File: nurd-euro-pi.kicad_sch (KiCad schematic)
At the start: 45 parts, among them J1 RPi_GPIO, J2 AudioJack2, J3 AudioJack2, J4 AudioJack2, J5 AudioJack2, J6 AudioJack2, J7 AudioJack2, Q1 2N3904, Q2 2N3904, U1 tl072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

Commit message: descriptions
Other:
- note added: "+/-5 => 0...3.3V"
- note added: "0...3 => +/- 5V"
- note added: "0/5V => 0/3.3V (don't break on -5V)"
- note added: "generate -5V"
- title: (none) -> Eurocrack Hat
- moved on the sheet: U6C
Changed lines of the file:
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@@
 (kicad_sch (version 20211123) (generator eeschema)
   (paper "A4")
+  (title_block
+    (title "Eurocrack Hat")
+  )
   (junction (at 78.74 33.02) (diameter 0) (color 0 0 0 0)
   )
@@
   (wire (pts (xy 74.93 87.63) (xy 80.01 87.63))
     (stroke (width 0) (type default) (color 0 0 0 0))
+  )
+  (text "generate -5V" (at 58.42 73.66 0)
+    (effects (font (size 1.27 1.27)) (justify left bottom))
+  )
+  (text "0...3 => +/- 5V" (at 55.88 146.05 0)
+    (effects (font (size 1.27 1.27)) (justify left bottom))
+  )
+  (text "0/5V => 0/3.3V (don't break on -5V)" (at 134.62 157.48 0)
+    (effects (font (size 1.27 1.27)) (justify left bottom))
+  )
+  (text "+/-5 => 0...3.3V" (at 60.96 16.51 0)
+    (effects (font (size 1.27 1.27)) (justify left bottom))
   )
   (symbol (lib_id "power:GND") (at 242.57 95.25 90) (unit 1)
@@
     (pin "2")
   )
-  (symbol (lib_id "Amplifier_Operational:MCP6002-xP") (at 193.04 27.94 0) (unit 3)
-    (in_bom yes) (on_board yes) (fields_autoplaced)
-    (property "Reference" "U6" (id 0) (at 191.77 26.6699 0)
-      (effects (font (size 1.27 1.27)) (justify left))
-    )
-    (property "Value" "tl072" (id 1) (at 191.77 29.2099 0)
-      (effects (font (size 1.27 1.27)) (justify left))
-    )
-    (property "Footprint" "Package_DIP:DIP-8_W7.62mm_Socket_LongPads" (id 2) (at 193.04 27.94 0)
-      (effects (font (size 1.27 1.27)) hide)
-    )
-    (property "Datasheet" "http://ww1.microchip.com/downloads/en/DeviceDoc/21733j.pdf" (id 3) (at 193.04 27.94 0)
+  (symbol (lib_id "Amplifier_Operational:MCP6002-xP") (at 92.71 24.13 90) (unit 3)
+    (in_bom yes) (on_board yes) (fields_autoplaced)
+    (property "Reference" "U6" (id 0) (at 91.4399 25.4 0)
+      (effects (font (size 1.27 1.27)) (justify left))
+    )
+    (property "Value" "tl072" (id 1) (at 93.9799 25.4 0)
+      (effects (font (size 1.27 1.27)) (justify left))
+    )
+    (property "Footprint" "Package_DIP:DIP-8_W7.62mm_Socket_LongPads" (id 2) (at 92.71 24.13 0)
+      (effects (font (size 1.27 1.27)) hide)
+    )
+    (property "Datasheet" "http://ww1.microchip.com/downloads/en/DeviceDoc/21733j.pdf" (id 3) (at 92.71 24.13 0)
       (effects (font (size 1.27 1.27)) hide)
     )
@@
     (pin "1")
   )
-  (symbol (lib_id "power:GND") (at 190.5 35.56 0) (unit 1)
-    (in_bom yes) (on_board yes) (fields_autoplaced)
-    (property "Reference" "#PWR0145" (id 0) (at 190.5 41.91 0)
-      (effects (font (size 1.27 1.27)) hide)
-    )
-    (property "Value" "GND" (id 1) (at 193.04 36.8299 0)
-      (effects (font (size 1.27 1.27)) (justify left))
-    )
-    (property "Footprint" "" (id 2) (at 190.5 35.56 0)
-      (effects (font (size 1.27 1.27)) hide)
-    )
-    (property "Datasheet" "" (id 3) (at 190.5 35.56 0)
+  (symbol (lib_id "power:GND") (at 100.33 26.67 90) (unit 1)
+    (in_bom yes) (on_board yes) (fields_autoplaced)
+    (property "Reference" "#PWR0145" (id 0) (at 106.68 26.67 0)
+      (effects (font (size 1.27 1.27)) hide)
+    )
+    (property "Value" "GND" (id 1) (at 101.5999 24.13 0)
+      (effects (font (size 1.27 1.27)) (justify left))
+    )
+    (property "Footprint" "" (id 2) (at 100.33 26.67 0)
+      (effects (font (size 1.27 1.27)) hide)
+    )
+    (property "Datasheet" "" (id 3) (at 100.33 26.67 0)
       (effects (font (size 1.27 1.27)) hide)
     )
@@
     (pin "8")
   )
-  (symbol (lib_id "power:+3.3V") (at 190.5 20.32 0) (unit 1)
-    (in_bom yes) (on_board yes) (fields_autoplaced)
-    (property "Reference" "#PWR0144" (id 0) (at 190.5 24.13 0)
-      (effects (font (size 1.27 1.27)) hide)
-    )
-    (property "Value" "+3.3V" (id 1) (at 193.04 19.0499 0)
-      (effects (font (size 1.27 1.27)) (justify left))
-    )
-    (property "Footprint" "" (id 2) (at 190.5 20.32 0)
-      (effects (font (size 1.27 1.27)) hide)
-    )
-    (property "Datasheet" "" (id 3) (at 190.5 20.32 0)
-      (effects (font (size 1.27 1.27)) hide)
-    )
+  (symbol (lib_id "power:+3.3V") (at 85.09 26.67 90) (unit 1)
+    (in_bom yes) (on_board yes) (fields_autoplaced)
+    (property "Reference" "#PWR0144" (id 0) (at 88.9 26.67 0)
+      (effects (font (size 1.27 1.27)) hide)
+    )
+    (property "Value" "+3.3V" (id 1) (at 83.8199 24.13 0)
+      (effects (font (size 1.27 1.27)) (justify left))
+    )
+    (property "Footprint" "" (id 2) (at 85.09 26.67 0)
+      (effects (font (size 1.27 1.27)) hide)
+    )
+    (property "Datasheet" "" (id 3) (at 85.09 26.67 0)
+      (effects (font (size 1.27 1.27)) hide)
+    )

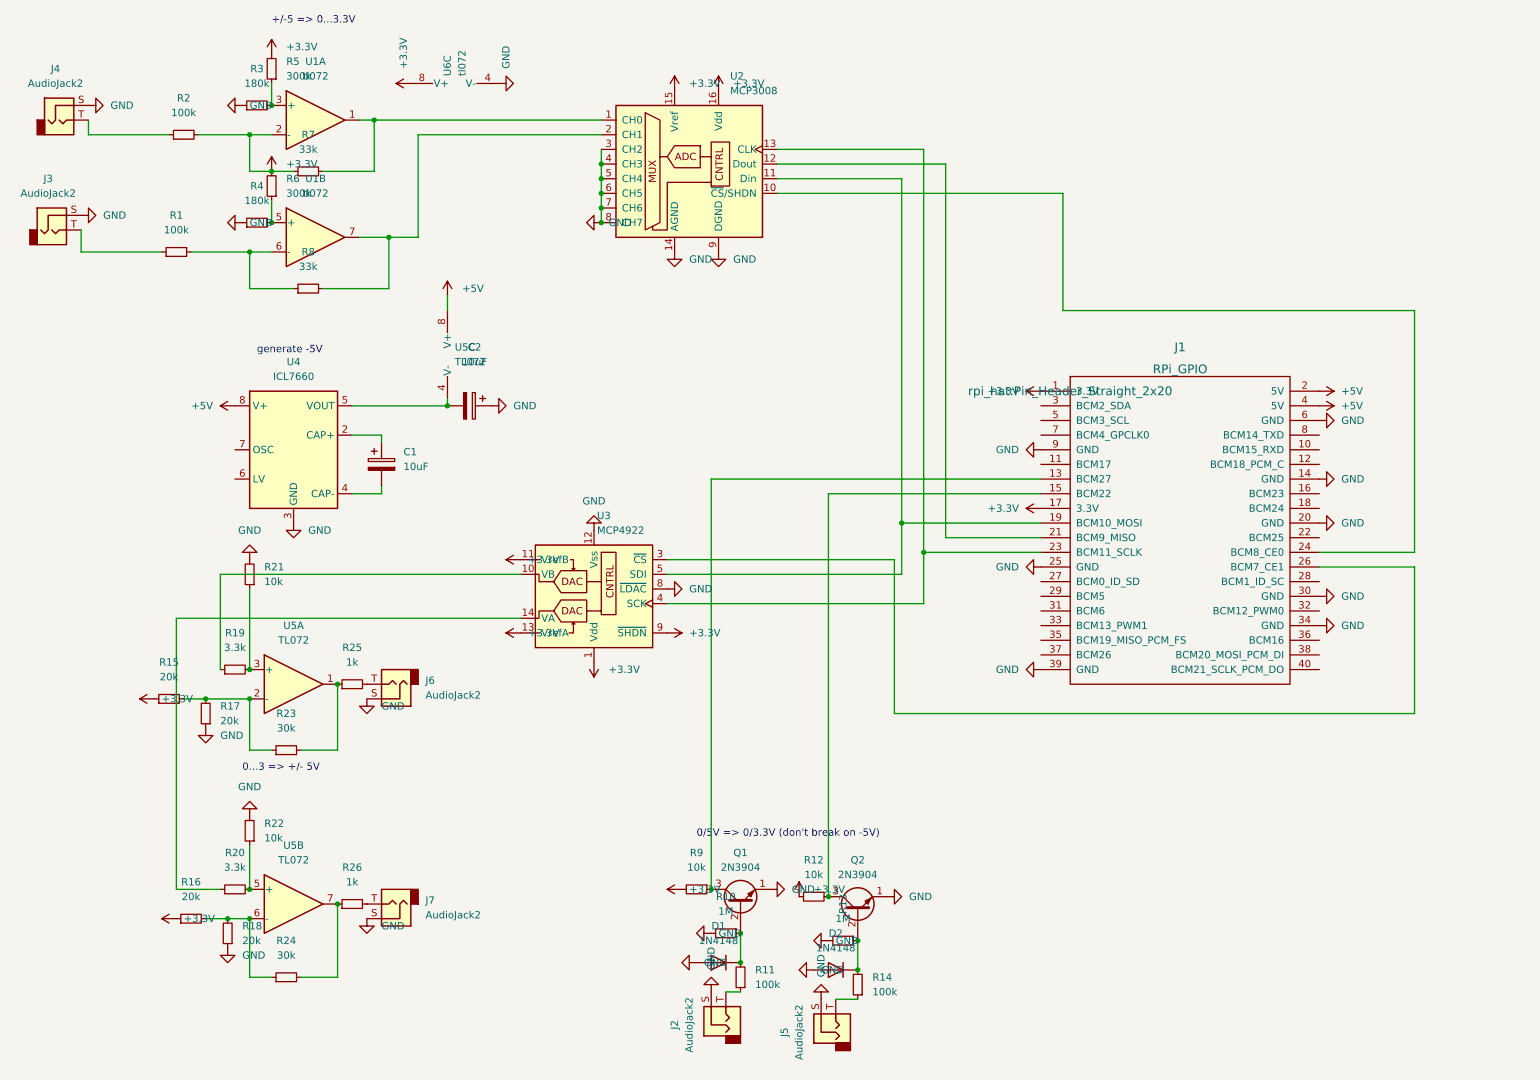
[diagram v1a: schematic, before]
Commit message: Added gate-out
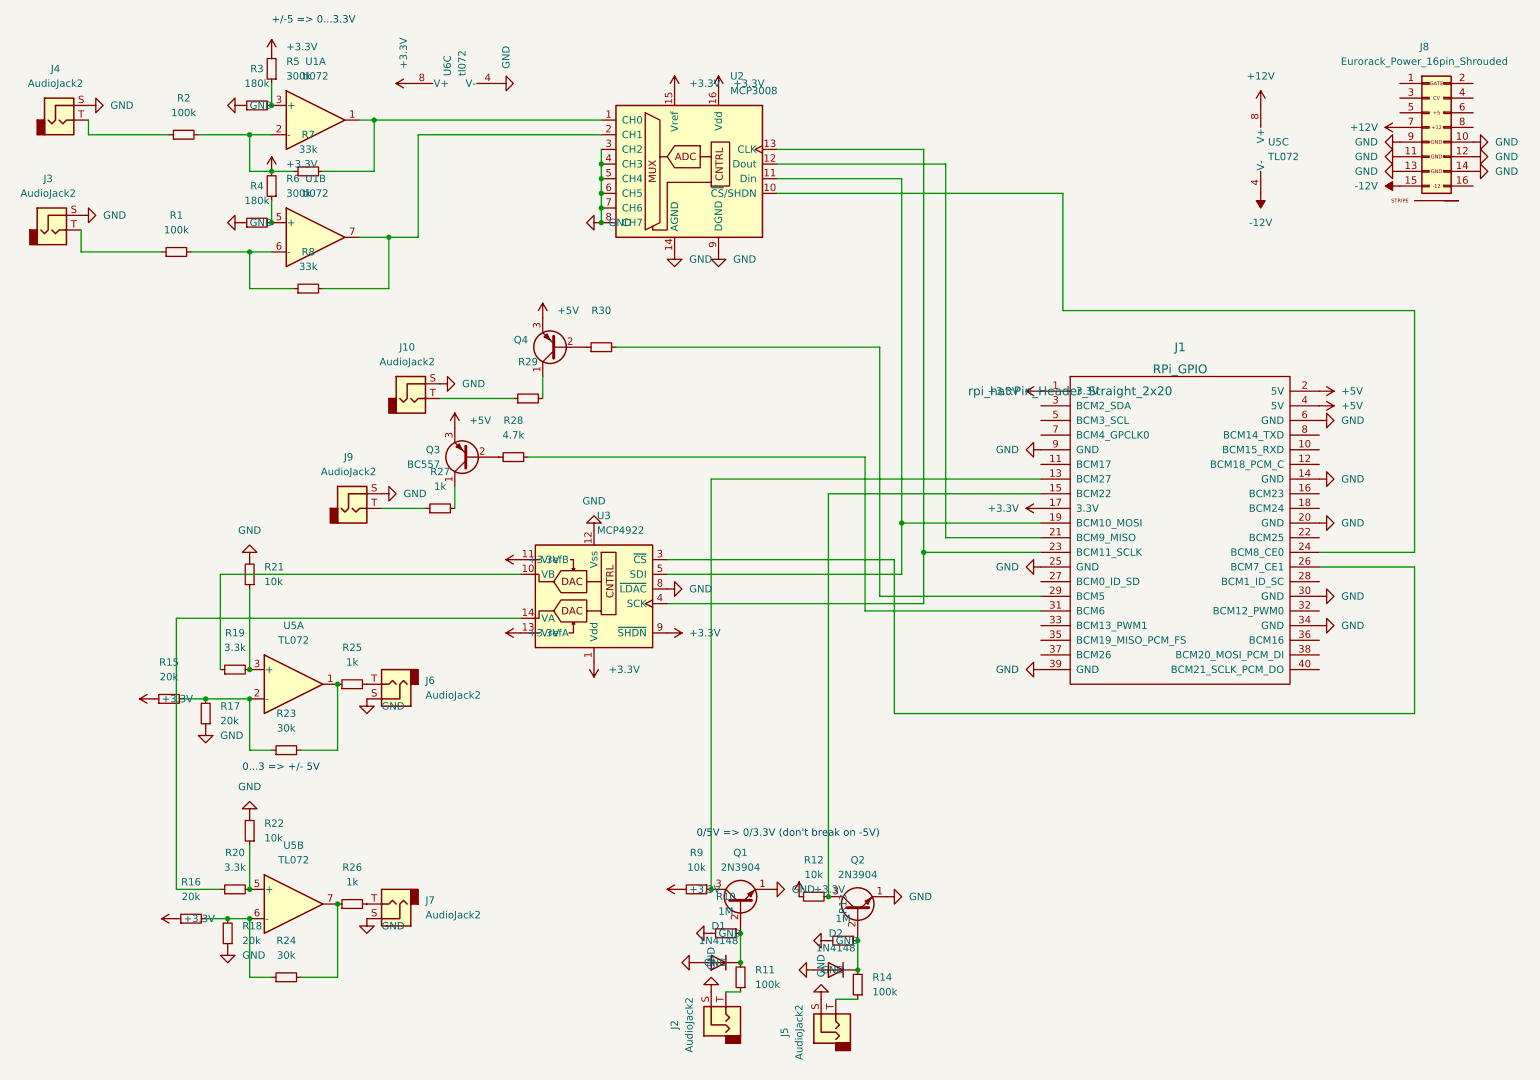
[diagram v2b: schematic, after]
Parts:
- removed C1, C2: 10uF, Capacitor_THT:CP_Radial_D5.0mm_P2.50mm, symbol Device:C_Polarized
- removed U4: ICL7660, Package_DIP:DIP-8_W7.62mm_Socket_LongPads, symbol Regulator_SwitchedCapacitor:ICL7660
- added J10, J9: AudioJack2, Connector_Audio:Jack_3.5mm_QingPu_WQP-PJ398SM_Vertical_CircularHoles, symbol Connector:AudioJack2
- added J8: Eurorack_Power_16pin_Shrouded, 4ms_Connector:Pins_2x08_2.54mm_TH_EuroPower_Shrouded, symbol eurorack_con:Eurorack_Power_16pin_Shrouded
- added Q3: BC557, Package_TO_SOT_THT:TO-92_Inline, symbol Transistor_BJT:BC557
- added Q4: (no value), symbol Transistor_BJT:BC557
- added R27: 1k, Resistor_THT:R_Axial_DIN0207_L6.3mm_D2.5mm_P7.62mm_Horizontal, symbol Device:R_Small
- added R28: 4.7k, Resistor_THT:R_Axial_DIN0207_L6.3mm_D2.5mm_P7.62mm_Horizontal, symbol Device:R_Small
- added R29, R30: (no value), symbol Device:R_Small
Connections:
- net +5V: now also Q3.3 (E), Q4.3 (E); no longer U5.8 (V+)
- net GND: now also J10.S, J8.10 (GND), J8.11 (GND), J8.12 (GND), J8.13 (-12), J8.14 (-12V), J8.9 (GND), J9.S
- net -12V: now reaches U5.4 (V-)
- net -12V: now also J8.15 (-12V)
- net at J1.29 (BCM5): now also R30.2
- net at J1.31 (BCM6): now also R28.2
- new net: Q4.2 (B), R30.1
- new net: J10.T, R29.1
- new net: Q3.1 (C), R27.2
- new net: Q3.2 (B), R28.1
- new net: J9.T, R27.1
- new net: Q4.1 (C), R29.2
- new net +12V: J8.7 (12V), U5.8 (V+)
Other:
- note removed: "generate -5V"
- company: (none) -> NURDspace (Flok)
- moved on the sheet: U5C
